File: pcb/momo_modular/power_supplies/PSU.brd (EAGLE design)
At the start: 7 x 7.1 mm, 24 parts, among them IC1 MAX1555

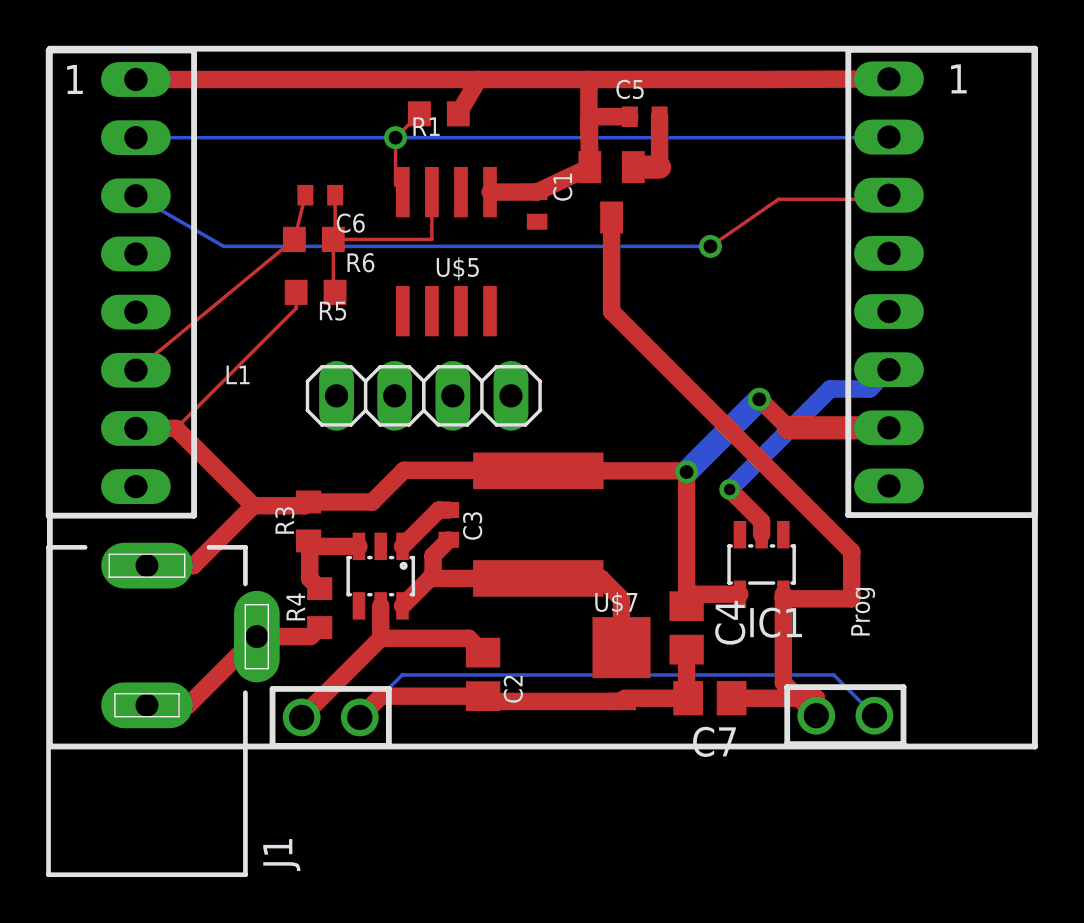
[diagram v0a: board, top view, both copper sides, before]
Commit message: Complete First draft of board layout
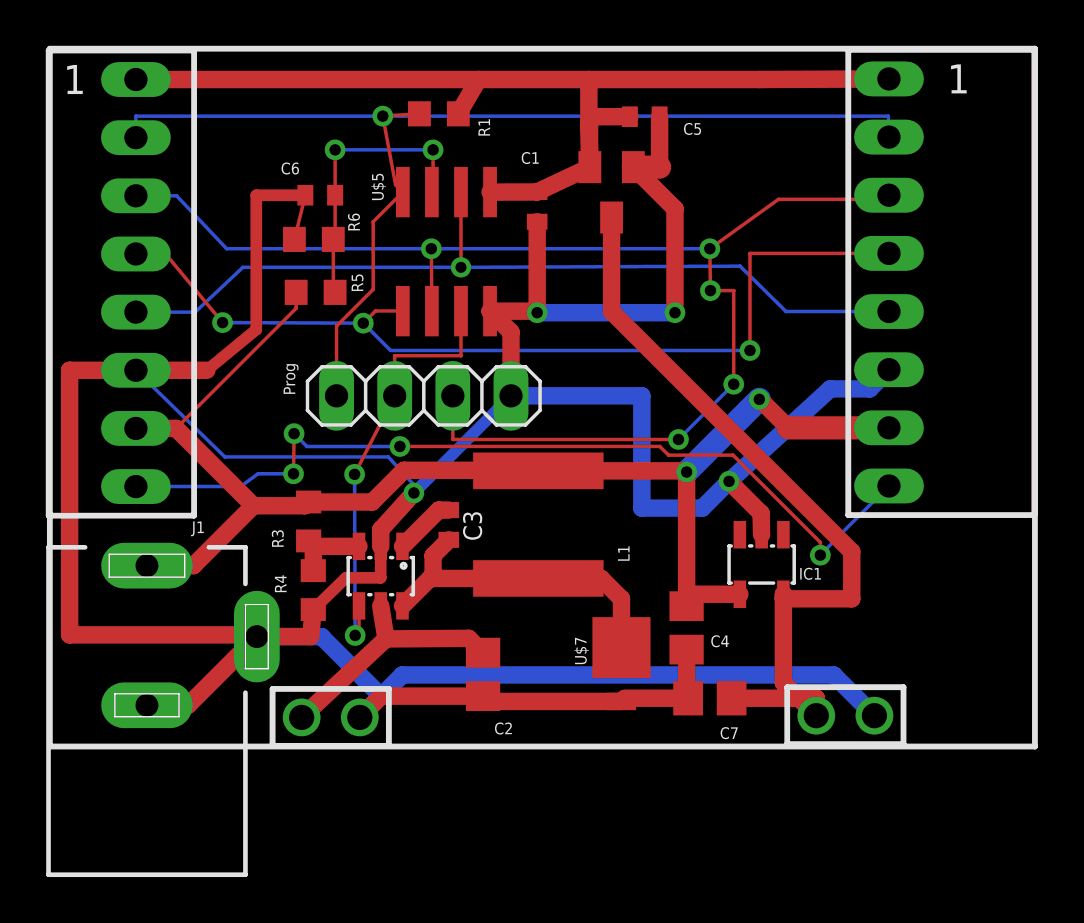
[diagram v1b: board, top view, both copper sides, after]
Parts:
- moved R4 0.84 mm to (11.4, 7.04)
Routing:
- net GND: track 76.0 -> 177.4 mm, vias 1 -> 4
- net DAT: track 0.00 -> 41.0 mm, vias 0 -> 3
- net PGND: track 0.00 -> 38.6 mm, vias 0 -> 4
- net IRQ: track 0.00 -> 37.8 mm, vias 0 -> 1
- net CLK: track 34.2 -> 59.5 mm, vias 1 -> 5
- net N$8: track 0.00 -> 18.9 mm, vias 0 -> 2
- net MCLR: track 36.9 -> 50.0 mm
- net N$5: track 10.7 -> 12.5 mm, vias 0 -> 2
- net N$6: track 4.61 -> 3.68 mm

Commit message: Updated schematic and layout to reflect capacitor changes
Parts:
- C4, C7: value 1 uF -> 1uF; device rcl:C0805 -> rcl:C0402
- moved C4 3.60 mm to (26.0, 8.53)
- moved C7 2.58 mm to (29.9, 4.62)
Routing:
- net N$1: track 34.6 -> 32.3 mm
- net GND: track 177.4 -> 179.5 mm, vias 4 -> 5
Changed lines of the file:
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@@
 <text x="25.2222" y="8.255" size="0.508" layer="21" rot="R90">L1</text>
 <text x="10.6172" y="15.5448" size="0.508" layer="21" rot="R90">Prog</text>
+<dimension x1="-0.1016" y1="30.6832" x2="-0.1016" y2="0.2032" x3="-3.7084" y3="15.4432" textsize="1.778" layer="20" dtype="horizontal" unit="inch"/>
+<dimension x1="-0.1016" y1="30.6832" x2="42.926" y2="30.6832" x3="21.4122" y3="34.2138" textsize="1.778" layer="20" dtype="horizontal" unit="inch"/>
 </plain>
 <attributes>
@@
 <attribute name="NAME" x="32.6136" y="7.493" size="0.508" layer="25"/>
 </element>
-<element name="C4" library="rcl" package="C0805" value="1 uF" x="27.7114" y="5.3848" smashed="yes" rot="R270">
-<attribute name="NAME" x="28.7528" y="4.5466" size="0.508" layer="25"/>
-</element>
-<element name="C7" library="rcl" package="C0805" value="1 uF" x="28.7274" y="2.3114" smashed="yes" rot="R180">
-<attribute name="NAME" x="29.9974" y="1.0414" size="0.508" layer="25" rot="R180"/>
-</element>
 <element name="U$1" library="components" package="MOMO-EDGE-SMALL-2M" value="MOMO-EDGE-POWER-M" x="12.1666" y="1.4732" smashed="yes" rot="R180"/>
 <element name="U$2" library="components" package="MOMO-EDGE-SMALL-2M" value="MOMO-EDGE-POWER-M" x="34.6456" y="1.5494" smashed="yes" rot="R180"/>
+<element name="C7" library="rcl" package="C0402" value="1uF" x="29.8704" y="4.6228" smashed="yes" rot="R180">
+<attribute name="NAME" x="30.8356" y="2.6924" size="0.508" layer="25" rot="R180"/>
+</element>
+<element name="C4" library="rcl" package="C0402" value="1uF" x="25.9588" y="8.5344" smashed="yes" rot="R270">
+<attribute name="NAME" x="26.797" y="9.4488" size="0.508" layer="25" rot="R270"/>
+</element>
 </elements>
 <signals>
@@
 <contactref element="IC1" pad="2"/>
 <contactref element="IC1" pad="2"/>
-<contactref element="C4" pad="2"/>
-<contactref element="C7" pad="2"/>
 <contactref element="U$1" pad="2"/>
 <contactref element="U$1" pad="2"/>
@@
 <wire x1="35.7124" y1="15.8242" x2="36.5506" y2="16.6624" width="0.762" layer="16"/>
 <via x="29.5656" y="11.7856" extent="1-16" drill="0.499325" diameter="0.1524"/>
-<wire x1="27.7114" y1="4.4348" x2="27.7114" y2="2.3774" width="0.762" layer="1"/>
-<wire x1="27.7114" y1="2.3774" x2="27.7774" y2="2.3114" width="0.1524" layer="1"/>
-<wire x1="27.7774" y1="2.3114" x2="25.0063" y2="2.3114" width="0.762" layer="1"/>
 <wire x1="25.0063" y1="2.3114" x2="24.8666" y2="2.1717" width="0.1524" layer="1"/>
 <wire x1="24.8666" y1="2.1717" x2="19.0525" y2="2.1717" width="0.762" layer="1"/>
 <wire x1="19.0525" y1="2.1717" x2="18.8214" y2="2.4028" width="0.1524" layer="1"/>
-<wire x1="35.9156" y1="1.5494" x2="34.1376" y2="3.3274" width="0.762" layer="16"/>
-<wire x1="34.1376" y1="3.3274" x2="15.2908" y2="3.3274" width="0.762" layer="16"/>
 <wire x1="15.2908" y1="3.3274" x2="14.3662" y2="2.4028" width="0.762" layer="16"/>
 <wire x1="14.3662" y1="2.4028" x2="13.4366" y2="1.4732" width="0.762" layer="16"/>
@@
 <wire x1="8.9408" y1="5.08" x2="8.9408" y2="4.9276" width="0.1524" layer="1"/>
 <wire x1="6.7564" y1="16.637" x2="3.6576" y2="16.637" width="0.762" layer="1"/>
+<contactref element="C7" pad="2"/>
+<contactref element="C4" pad="2"/>
+<wire x1="35.9156" y1="1.5494" x2="34.1884" y2="3.2766" width="0.762" layer="16"/>
+<wire x1="34.1884" y1="3.2766" x2="27.432" y2="3.2766" width="0.762" layer="16"/>
+<wire x1="27.432" y1="3.2766" x2="27.432" y2="4.5974" width="0.762" layer="16"/>
+<wire x1="27.432" y1="4.5974" x2="27.4574" y2="4.6228" width="0.762" layer="16"/>
+<wire x1="27.4574" y1="4.6228" x2="29.2204" y2="4.6228" width="0.762" layer="1"/>
+<via x="27.4574" y="4.6228" extent="1-16" drill="0.496971875"/>
+<wire x1="25.9588" y1="7.8844" x2="27.4574" y2="6.3858" width="0.762" layer="1"/>
+<wire x1="27.4574" y1="6.3858" x2="27.4574" y2="4.6228" width="0.762" layer="1"/>
+<wire x1="27.432" y1="3.2766" x2="27.3812" y2="3.3274" width="0.762" layer="16"/>
+<wire x1="27.3812" y1="3.3274" x2="15.2908" y2="3.3274" width="0.762" layer="16"/>
 </signal>
 <signal name="VCCINT">
@@
 <contactref element="R3" pad="2"/>
 <contactref element="IC1" pad="4"/>
-<contactref element="C4" pad="1"/>
 <contactref element="U$10" pad="V4."/>
 <contactref element="U$11" pad="V4"/>
 <contactref element="R5" pad="2"/>
-<wire x1="30.038" y1="6.8534" x2="27.813" y2="6.8534" width="0.762" layer="1"/>
-<wire x1="27.813" y1="6.8534" x2="27.7114" y2="6.3348" width="0.762" layer="1"/>
 <wire x1="4.1402" y1="8.1038" x2="6.1734" y2="8.1038" width="0.762" layer="1"/>
 <wire x1="6.1734" y1="8.1038" x2="8.7884" y2="10.7188" width="0.762" layer="1"/>
@@
 <wire x1="21.2344" y1="12.2438" x2="27.7114" y2="12.2438" width="0.762" layer="1"/>
 <wire x1="27.7114" y1="12.2438" x2="27.7114" y2="12.192" width="0.762" layer="1"/>
-<wire x1="27.7114" y1="12.192" x2="27.7114" y2="6.3348" width="0.762" layer="1"/>
 <wire x1="36.5506" y1="14.1224" x2="32.1564" y2="14.1224" width="1.016" layer="1"/>
 <wire x1="32.1564" y1="14.1224" x2="30.8864" y2="15.3924" width="0.762" layer="1"/>
@@
 <wire x1="5.4102" y1="14.097" x2="10.6562" y2="19.343" width="0.1524" layer="1"/>
 <wire x1="10.6562" y1="19.343" x2="10.6562" y2="20.0406" width="0.1524" layer="1"/>
+<contactref element="C4" pad="1"/>
+<wire x1="30.038" y1="6.8534" x2="27.7114" y2="9.18" width="0.762" layer="1"/>
+<wire x1="27.7114" y1="9.18" x2="27.7114" y2="9.3472" width="0.762" layer="1"/>
+<wire x1="27.7114" y1="9.3472" x2="27.7114" y2="12.192" width="0.762" layer="1"/>
+<wire x1="25.9588" y1="9.1844" x2="26.1216" y2="9.3472" width="0.762" layer="1"/>
+<wire x1="26.1216" y1="9.3472" x2="27.7114" y2="9.3472" width="0.762" layer="1"/>
 </signal>
 <signal name="+18V">
@@
 <contactref element="U$2" pad="1"/>
 <contactref element="U$9" pad="3"/>
-<contactref element="C7" pad="1"/>
 <wire x1="33.3756" y1="1.5494" x2="33.3456" y2="1.5494" width="0.762" layer="1"/>
-<wire x1="29.6774" y1="2.3114" x2="33.3756" y2="2.3114" width="0.762" layer="1"/>
 <wire x1="33.3756" y1="2.3114" x2="33.3756" y2="1.5494" width="0.762" layer="1"/>
 <wire x1="24.4348" y1="23.3094" x2="24.4348" y2="19.2024" width="0.762" layer="1"/>
@@
 <wire x1="34.925" y1="6.6548" x2="31.938" y2="6.6548" width="0.762" layer="1"/>
 <wire x1="31.938" y1="6.6548" x2="31.938" y2="6.8534" width="0.762" layer="1"/>
-<wire x1="31.938" y1="6.8534" x2="31.938" y2="2.987" width="0.762" layer="1"/>
+<wire x1="31.938" y1="6.8534" x2="31.938" y2="6.1468" width="0.762" layer="1"/>
+<wire x1="31.938" y1="4.6228" x2="31.938" y2="2.987" width="0.762" layer="1"/>
 <wire x1="31.938" y1="2.987" x2="33.3756" y2="1.5494" width="0.762" layer="1"/>
+<contactref element="C7" pad="1"/>
+<wire x1="30.5204" y1="4.6228" x2="31.938" y2="4.6228" width="0.762" layer="1"/>
+<wire x1="31.938" y1="4.6228" x2="31.938" y2="6.1468" width="0.762" layer="1"/>
 </signal>
 </signals>
